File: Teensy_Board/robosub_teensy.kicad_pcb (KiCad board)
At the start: 2 copper layers, 51 parts, among them IC1 TEENSY_4.1, J1 Conn_01x03_Pin, J10 Conn_01x02_Pin, J11 Conn_01x02_Pin, J12 Conn_01x04_Pin, J13 Conn_01x04_Pin, J14 Conn_01x04_Pin, J15 Conn_01x04_Pin, J16 Conn_01x04_Pin, J17 Conn_01x04_Pin, J18 Conn_01x04_Pin, J19 Conn_01x04_Pin, J2 Conn_01x03_Pin, J20 Conn_01x04_Pin, J21 Conn_01x04_Pin, J22 Conn_01x06_Pin, J23 Conn_01x06_Pin, J24 Conn_01x06_Pin, J25 Conn_01x01_Pin, J26 Conn_01x01_Pin, J27 Conn_01x01_Pin, J28 Conn_01x01_Pin, J29 Conn_01x01_Pin, J3 Conn_01x03_Pin, J30 Conn_01x01_Pin, J31 Conn_01x01_Pin, J32 Conn_01x01_Pin, J33 Conn_01x01_Pin, J34 Conn_01x01_Pin, J35 Conn_01x01_Pin, J36 Conn_01x01_Pin, J37 Conn_01x01_Pin, J38 Conn_01x01_Pin, J39 Conn_01x01_Pin, J4 Conn_01x03_Pin, J40 Conn_01x01_Pin, J41 Conn_01x01_Pin, J42 Conn_01x01_Pin, J43 Conn_01x01_Pin, J44 Conn_01x01_Pin, J45 Conn_01x01_Pin, J46 Conn_01x01_Pin, J47 Conn_01x01_Pin, J48 Conn_01x10_Pin, J49 Conn_01x10_Pin, J5 Conn_01x03_Pin, J50 Conn_01x10_Pin, J6 Conn_01x03_Pin, J7 Conn_01x03_Pin, J8 Conn_01x03_Pin, J9 Conn_01x02_Pin

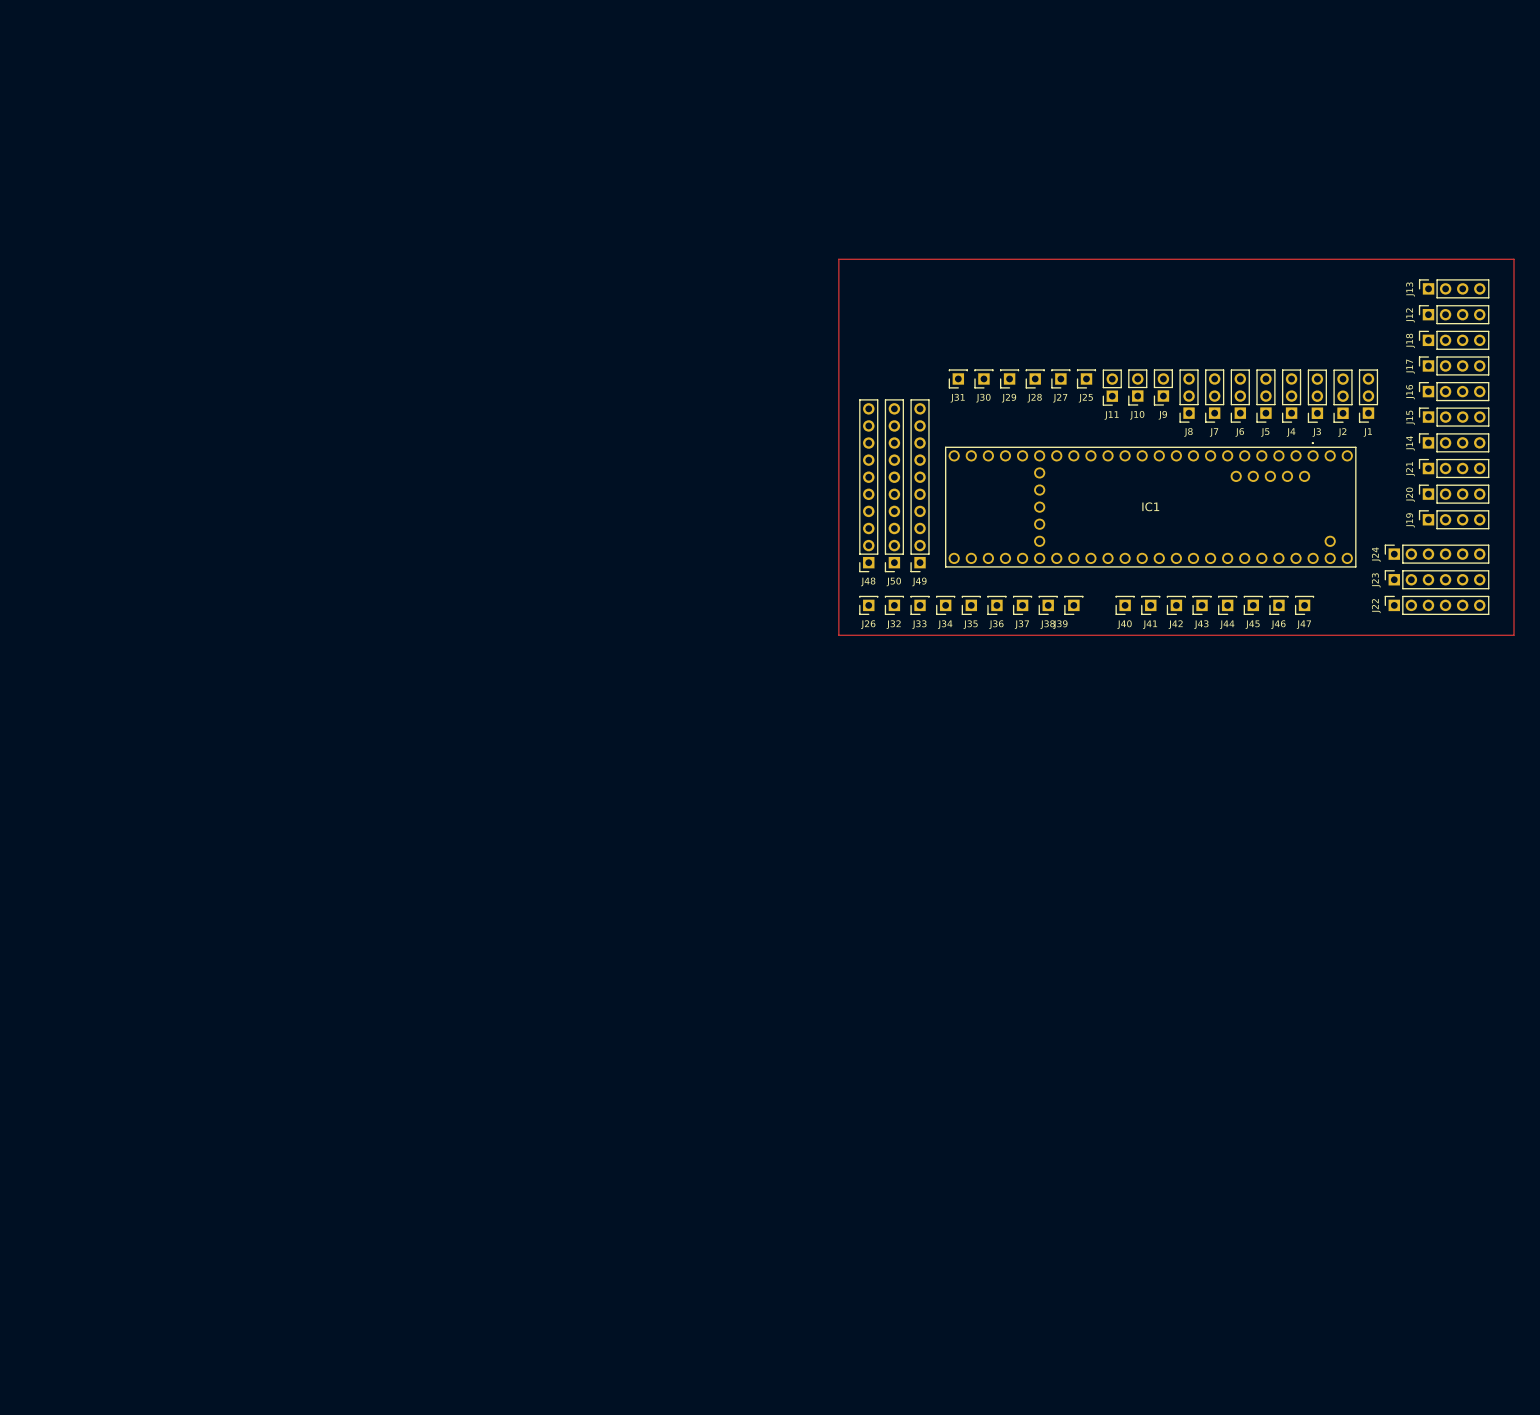
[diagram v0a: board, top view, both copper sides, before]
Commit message: teensy board schematic
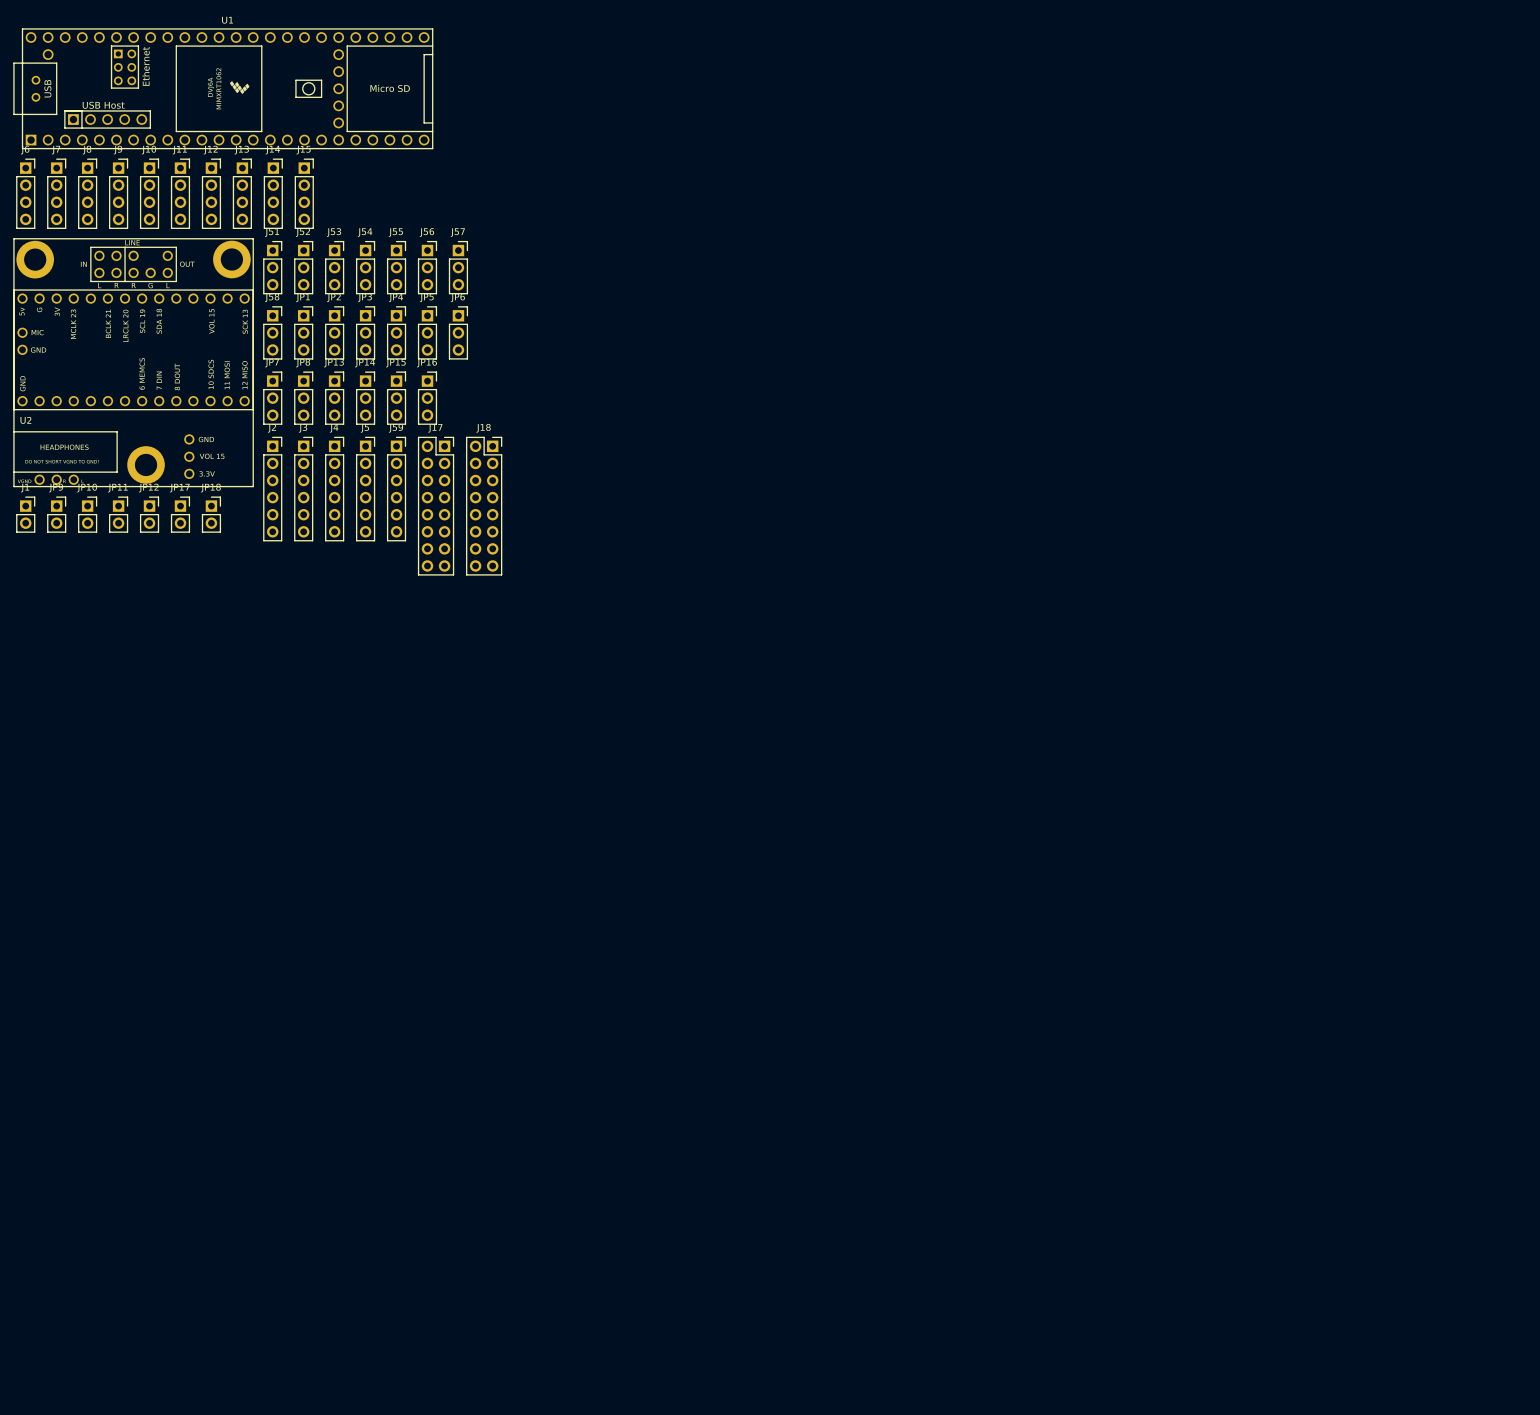
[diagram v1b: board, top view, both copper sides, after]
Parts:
- removed IC1: TEENSY_4.1, KiCad:TEENSY41
- removed J16, J19, J20, J21: Conn_01x04_Pin, Connector_PinSocket_2.54mm:PinSocket_1x04_P2.54mm_Vertical
- removed J22, J23, J24: Conn_01x06_Pin, Connector_PinSocket_2.54mm:PinSocket_1x06_P2.54mm_Vertical
- removed J25, J26, J27, J28, J29, J30, J31, J32, J33, J34, J35, J36, J37, J38, J39, J40, J41, J42, J43, J44, J45, J46, J47: Conn_01x01_Pin, Connector_PinSocket_2.54mm:PinSocket_1x01_P2.54mm_Vertical
- removed J48, J49, J50: Conn_01x10_Pin, Connector_PinSocket_2.54mm:PinSocket_1x10_P2.54mm_Vertical
- added J51: Thruster_1, Connector_PinSocket_2.54mm:PinSocket_1x03_P2.54mm_Vertical, F.Cu at (66.4, 52.7)
- added J52: Thruster_2, Connector_PinSocket_2.54mm:PinSocket_1x03_P2.54mm_Vertical, F.Cu at (71.0, 52.7)
- added J53: Thruster_3, Connector_PinSocket_2.54mm:PinSocket_1x03_P2.54mm_Vertical, F.Cu at (75.6, 52.7)
- added J54: Thruster_6, Connector_PinSocket_2.54mm:PinSocket_1x03_P2.54mm_Vertical, F.Cu at (80.2, 52.7)
- added J55: Thruster_5, Connector_PinSocket_2.54mm:PinSocket_1x03_P2.54mm_Vertical, F.Cu at (84.8, 52.7)
- added J56: Thruster_4, Connector_PinSocket_2.54mm:PinSocket_1x03_P2.54mm_Vertical, F.Cu at (89.4, 52.7)
- added J57: Thruster_8, Connector_PinSocket_2.54mm:PinSocket_1x03_P2.54mm_Vertical, F.Cu at (94.0, 52.7)
- added J58: Thruster_7, Connector_PinSocket_2.54mm:PinSocket_1x03_P2.54mm_Vertical, F.Cu at (66.4, 62.4)
- added J59: PixHawk PM02, Connector_PinSocket_2.54mm:PinSocket_1x06_P2.54mm_Vertical, F.Cu at (84.8, 81.8)
- added JP1: Jumper_3_Bridged12, Connector_PinSocket_2.54mm:PinSocket_1x03_P2.54mm_Vertical, F.Cu at (71.0, 62.4)
- added JP10: Jumper_2_Open, Connector_PinSocket_2.54mm:PinSocket_1x02_P2.54mm_Vertical, F.Cu at (38.9, 90.7)
- added JP11: Jumper_2_Open, Connector_PinSocket_2.54mm:PinSocket_1x02_P2.54mm_Vertical, F.Cu at (43.5, 90.7)
- added JP12: Jumper_2_Open, Connector_PinSocket_2.54mm:PinSocket_1x02_P2.54mm_Vertical, F.Cu at (48.0, 90.7)
- added JP13: Jumper_3_Bridged12, Connector_PinSocket_2.54mm:PinSocket_1x03_P2.54mm_Vertical, F.Cu at (75.6, 72.1)
- added JP14: Jumper_3_Bridged12, Connector_PinSocket_2.54mm:PinSocket_1x03_P2.54mm_Vertical, F.Cu at (80.2, 72.1)
- added JP15: Jumper_3_Bridged12, Connector_PinSocket_2.54mm:PinSocket_1x03_P2.54mm_Vertical, F.Cu at (84.8, 72.1)
- added JP16: Jumper_3_Bridged12, Connector_PinSocket_2.54mm:PinSocket_1x03_P2.54mm_Vertical, F.Cu at (89.4, 72.1)
- added JP17: Jumper_2_Open, Connector_PinSocket_2.54mm:PinSocket_1x02_P2.54mm_Vertical, F.Cu at (52.6, 90.7)
- added JP18: Jumper_2_Open, Connector_PinSocket_2.54mm:PinSocket_1x02_P2.54mm_Vertical, F.Cu at (57.2, 90.7)
- added JP2: Jumper_3_Bridged12, Connector_PinSocket_2.54mm:PinSocket_1x03_P2.54mm_Vertical, F.Cu at (75.6, 62.4)
- added JP3: Jumper_3_Bridged12, Connector_PinSocket_2.54mm:PinSocket_1x03_P2.54mm_Vertical, F.Cu at (80.2, 62.4)
- added JP4: Jumper_3_Bridged12, Connector_PinSocket_2.54mm:PinSocket_1x03_P2.54mm_Vertical, F.Cu at (84.8, 62.4)
- added JP5: Jumper_3_Bridged12, Connector_PinSocket_2.54mm:PinSocket_1x03_P2.54mm_Vertical, F.Cu at (89.4, 62.4)
- added JP6: Jumper_3_Bridged12, Connector_PinSocket_2.54mm:PinSocket_1x03_P2.54mm_Vertical, F.Cu at (94.0, 62.4)
- added JP7: Jumper_3_Bridged12, Connector_PinSocket_2.54mm:PinSocket_1x03_P2.54mm_Vertical, F.Cu at (66.4, 72.1)
- added JP8: Jumper_3_Bridged12, Connector_PinSocket_2.54mm:PinSocket_1x03_P2.54mm_Vertical, F.Cu at (71.0, 72.1)
- added JP9: Jumper_2_Open, Connector_PinSocket_2.54mm:PinSocket_1x02_P2.54mm_Vertical, F.Cu at (34.2, 90.7)
- added U1: Teensy4.1, teensy:Teensy41, F.Cu at (59.6, 28.6)
- added U2: Teensy4.0_AudioShield_REVD, teensy_audio_shield:4.0audioshield, F.Cu at (29.2, 75.0)
- J1: value Conn_01x03_Pin -> UART; footprint Connector_PinSocket_2.54mm:PinSocket_1x03_P2.54mm_Vertical -> Connector_PinSocket_2.54mm:PinSocket_1x02_P2.54mm_Vertical
- J10: value Conn_01x02_Pin -> I2C1_BUS5; footprint Connector_PinSocket_2.54mm:PinSocket_1x02_P2.54mm_Vertical -> Connector_PinSocket_2.54mm:PinSocket_1x04_P2.54mm_Vertical
- J11: value Conn_01x02_Pin -> I2C1_BUS7; footprint Connector_PinSocket_2.54mm:PinSocket_1x02_P2.54mm_Vertical -> Connector_PinSocket_2.54mm:PinSocket_1x04_P2.54mm_Vertical
- J12: value Conn_01x04_Pin -> I2C1_BUS6
- J13: value Conn_01x04_Pin -> I2C1_BUS8
- J14: value Conn_01x04_Pin -> I2C2_BUS1
- J15: value Conn_01x04_Pin -> I2C3_BUS1
- J17: value Conn_01x04_Pin -> 3.3V Power; footprint Connector_PinSocket_2.54mm:PinSocket_1x04_P2.54mm_Vertical -> Connector_PinSocket_2.54mm:PinSocket_2x08_P2.54mm_Vertical
- J18: value Conn_01x04_Pin -> 5V Power; footprint Connector_PinSocket_2.54mm:PinSocket_1x04_P2.54mm_Vertical -> Connector_PinSocket_2.54mm:PinSocket_2x08_P2.54mm_Vertical
- J2: value Conn_01x03_Pin -> SPI_BUS1; footprint Connector_PinSocket_2.54mm:PinSocket_1x03_P2.54mm_Vertical -> Connector_PinSocket_2.54mm:PinSocket_1x06_P2.54mm_Vertical
- J3: value Conn_01x03_Pin -> SPI_BUS2; footprint Connector_PinSocket_2.54mm:PinSocket_1x03_P2.54mm_Vertical -> Connector_PinSocket_2.54mm:PinSocket_1x06_P2.54mm_Vertical
- J4: value Conn_01x03_Pin -> SPI_BUS3; footprint Connector_PinSocket_2.54mm:PinSocket_1x03_P2.54mm_Vertical -> Connector_PinSocket_2.54mm:PinSocket_1x06_P2.54mm_Vertical
- J5: value Conn_01x03_Pin -> SPI_BUS4; footprint Connector_PinSocket_2.54mm:PinSocket_1x03_P2.54mm_Vertical -> Connector_PinSocket_2.54mm:PinSocket_1x06_P2.54mm_Vertical
- J6: value Conn_01x03_Pin -> I2C1_BUS1; footprint Connector_PinSocket_2.54mm:PinSocket_1x03_P2.54mm_Vertical -> Connector_PinSocket_2.54mm:PinSocket_1x04_P2.54mm_Vertical
- J7: value Conn_01x03_Pin -> I2C1_BUS2; footprint Connector_PinSocket_2.54mm:PinSocket_1x03_P2.54mm_Vertical -> Connector_PinSocket_2.54mm:PinSocket_1x04_P2.54mm_Vertical
- J8: value Conn_01x03_Pin -> I2C1_BUS3; footprint Connector_PinSocket_2.54mm:PinSocket_1x03_P2.54mm_Vertical -> Connector_PinSocket_2.54mm:PinSocket_1x04_P2.54mm_Vertical
- J9: value Conn_01x02_Pin -> I2C1_BUS4; footprint Connector_PinSocket_2.54mm:PinSocket_1x02_P2.54mm_Vertical -> Connector_PinSocket_2.54mm:PinSocket_1x04_P2.54mm_Vertical
- moved J1 200.0 mm to (29.6, 90.7), turned to 0 degrees
- moved J6 184.1 mm to (29.6, 40.4), turned to 0 degrees
- moved J12 182.2 mm to (57.2, 40.4), turned to 0 degrees
- moved J13 177.2 mm to (61.9, 40.4), turned to 0 degrees
- moved J14 176.5 mm to (66.5, 40.4), turned to 0 degrees
- moved J7 175.9 mm to (34.2, 40.4), turned to 0 degrees
- moved J15 171.1 mm to (71.0, 40.4), turned to 0 degrees
- moved J8 167.7 mm to (38.9, 40.4), turned to 0 degrees
- moved J2 159.1 mm to (66.4, 81.8), turned to 0 degrees
- moved J9 158.9 mm to (43.5, 40.4), turned to 0 degrees
- moved J3 150.7 mm to (71.0, 81.8), turned to 0 degrees
- moved J10 150.7 mm to (48.0, 40.4), turned to 0 degrees
- moved J17 146.7 mm to (91.9, 81.8), turned to 0 degrees
- moved J11 142.6 mm to (52.6, 40.4), turned to 0 degrees
- moved J4 142.3 mm to (75.6, 81.8), turned to 0 degrees
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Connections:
- J1 pad 1: Net-(IC1-OUT2) -> UART_RX
- J1 pad 2: unconnected-(J1-Pin_2-Pad2) -> UART_TX
- J10 pad 1: Net-(IC1-A11) -> +3.3V
- J10 pad 2: Net-(IC1-GND_6) -> I2C1_SCL
- J11 pad 1: Net-(IC1-A12) -> +3.3V
- J11 pad 2: Net-(IC1-GND_6) -> I2C1_SCL
- J12 pad 1: Net-(IC1-A4) -> +3.3V
- J12 pad 2: Net-(IC1-A5) -> I2C1_SCL
- J12 pad 3: Net-(IC1-3.3V_1) -> I2C1_SDA
- J12 pad 4: Net-(IC1-GND_6) -> GND
- J13 pad 1: Net-(IC1-A4) -> +3.3V
- J13 pad 2: Net-(IC1-A5) -> I2C1_SCL
- J13 pad 3: Net-(IC1-3.3V_1) -> I2C1_SDA
- J13 pad 4: Net-(IC1-GND_6) -> GND
- J14 pad 1: Net-(IC1-A4) -> Net-(J14-Pin_1)
- J14 pad 2: Net-(IC1-A5) -> I2C2_SCL
- J14 pad 3: Net-(IC1-3.3V_1) -> I2C2_SDA
- J14 pad 4: Net-(IC1-GND_6) -> GND
- J15 pad 1: Net-(IC1-A4) -> Net-(J15-Pin_1)
- J15 pad 2: Net-(IC1-A5) -> I2C3_SCL
- J15 pad 3: Net-(IC1-3.3V_1) -> I2C3_SDA
- J15 pad 4: Net-(IC1-GND_6) -> GND
- J17 pad 1: Net-(IC1-A4) -> +3.3V
- J17 pad 2: Net-(IC1-A5) -> +3.3V
- J17 pad 3: Net-(IC1-3.3V_1) -> +3.3V
- J17 pad 4: Net-(IC1-GND_6) -> +3.3V
- J18 pad 1: Net-(IC1-A4) -> +5V
- J18 pad 2: Net-(IC1-A5) -> +5V
- J18 pad 3: Net-(IC1-3.3V_1) -> +5V
- J18 pad 4: Net-(IC1-GND_6) -> +5V
- J2 pad 2: unconnected-(J2-Pin_2-Pad2) -> SPI_MOSI
- J2 pad 3: Net-(IC1-GND_6) -> SPI_MISO
- J3 pad 2: unconnected-(J3-Pin_2-Pad2) -> SPI_MOSI
- J3 pad 3: Net-(IC1-GND_6) -> SPI_MISO
- J4 pad 1: Net-(IC1-IN2) -> +3.3V
- J4 pad 2: unconnected-(J4-Pin_2-Pad2) -> SPI_MOSI
- J4 pad 3: Net-(IC1-GND_6) -> SPI_MISO
- J5 pad 1: Net-(IC1-OUT1D) -> +3.3V
- J5 pad 2: unconnected-(J5-Pin_2-Pad2) -> SPI_MOSI
- J5 pad 3: Net-(IC1-GND_6) -> SPI_MISO
- J6 pad 2: unconnected-(J6-Pin_2-Pad2) -> I2C1_SCL
- J6 pad 3: Net-(IC1-GND_6) -> I2C1_SDA
- J7 pad 2: unconnected-(J7-Pin_2-Pad2) -> I2C1_SCL
- J7 pad 3: Net-(IC1-GND_6) -> I2C1_SDA
- J8 pad 2: unconnected-(J8-Pin_2-Pad2) -> I2C1_SCL
- J8 pad 3: Net-(IC1-GND_6) -> I2C1_SDA
- J9 pad 2: Net-(IC1-GND_6) -> I2C1_SCL

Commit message: v1 ok2fab
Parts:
- removed J15: I2C3_BUS1, Connector_PinSocket_2.54mm:PinSocket_1x04_P2.54mm_Vertical
- removed J51: Thruster_1, Connector_PinSocket_2.54mm:PinSocket_1x03_P2.54mm_Vertical
- removed J52: Thruster_2, Connector_PinSocket_2.54mm:PinSocket_1x03_P2.54mm_Vertical
- removed J53: Thruster_3, Connector_PinSocket_2.54mm:PinSocket_1x03_P2.54mm_Vertical
- removed J54: Thruster_6, Connector_PinSocket_2.54mm:PinSocket_1x03_P2.54mm_Vertical
- removed J55: Thruster_5, Connector_PinSocket_2.54mm:PinSocket_1x03_P2.54mm_Vertical
- removed J56: Thruster_4, Connector_PinSocket_2.54mm:PinSocket_1x03_P2.54mm_Vertical
- removed J57: Thruster_8, Connector_PinSocket_2.54mm:PinSocket_1x03_P2.54mm_Vertical
- removed J58: Thruster_7, Connector_PinSocket_2.54mm:PinSocket_1x03_P2.54mm_Vertical
- removed J59: PixHawk PM02, Connector_PinSocket_2.54mm:PinSocket_1x06_P2.54mm_Vertical
- removed JP5, JP6: Jumper_3_Bridged12, Connector_PinSocket_2.54mm:PinSocket_1x03_P2.54mm_Vertical
- added H1: MountingHole, MountingHole:MountingHole_3.2mm_M3, F.Cu at (135.8, 167.2)
- added H2: MountingHole, MountingHole:MountingHole_3.2mm_M3, F.Cu at (195.8, 212.2)
- added H3: MountingHole, MountingHole:MountingHole_3.2mm_M3, F.Cu at (240.8, 212.2)
- added J19: BUS4, Connector_PinSocket_2.54mm:PinSocket_1x04_P2.54mm_Vertical, F.Cu at (245.8, 162.1)
- added J20: BUS5, Connector_PinSocket_2.54mm:PinSocket_1x04_P2.54mm_Vertical, F.Cu at (153.3, 161.4)
- added J21: BUS6, Connector_PinSocket_2.54mm:PinSocket_1x04_P2.54mm_Vertical, F.Cu at (157.3, 161.4)
- added J22: SPI1, Connector_PinSocket_2.54mm:PinSocket_1x06_P2.54mm_Vertical, F.Cu at (181.2, 161.5)
- added J23: SPI2, Connector_PinSocket_2.54mm:PinSocket_1x06_P2.54mm_Vertical, F.Cu at (185.8, 161.5)
- added J24: I2C_2, Connector_PinSocket_2.54mm:PinSocket_1x04_P2.54mm_Vertical, F.Cu at (165.1, 161.3)
- added J25: I2C_3, Connector_PinSocket_2.54mm:PinSocket_1x04_P2.54mm_Vertical, F.Cu at (169.1, 161.3)
- added J26: SPI3, Connector_PinSocket_2.54mm:PinSocket_1x06_P2.54mm_Vertical, F.Cu at (190.5, 161.5)
- added J27: SPI4, Connector_PinSocket_2.54mm:PinSocket_1x06_P2.54mm_Vertical, F.Cu at (195.1, 161.5)
- J1: value UART -> T1; footprint Connector_PinSocket_2.54mm:PinSocket_1x02_P2.54mm_Vertical -> Connector_PinSocket_2.54mm:PinSocket_1x03_P2.54mm_Vertical
- J10: value I2C1_BUS5 -> PixHawk PM02; footprint Connector_PinSocket_2.54mm:PinSocket_1x04_P2.54mm_Vertical -> Connector_PinSocket_2.54mm:PinSocket_1x06_P2.54mm_Vertical
- J11: value I2C1_BUS7 -> 3.3V Power; footprint Connector_PinSocket_2.54mm:PinSocket_1x04_P2.54mm_Vertical -> Connector_PinSocket_2.54mm:PinSocket_2x08_P2.54mm_Vertical
- J12: value I2C1_BUS6 -> 5V Power; footprint Connector_PinSocket_2.54mm:PinSocket_1x04_P2.54mm_Vertical -> Connector_PinSocket_2.54mm:PinSocket_2x08_P2.54mm_Vertical
- J13: value I2C1_BUS8 -> BUS1
- J14: value I2C2_BUS1 -> BUS2
- J17: value 3.3V Power -> Digital Pins; footprint Connector_PinSocket_2.54mm:PinSocket_2x08_P2.54mm_Vertical -> Connector_PinSocket_2.54mm:PinSocket_2x11_P2.54mm_Vertical
- J18: value 5V Power -> BUS3; footprint Connector_PinSocket_2.54mm:PinSocket_2x08_P2.54mm_Vertical -> Connector_PinSocket_2.54mm:PinSocket_1x04_P2.54mm_Vertical
- J2: value SPI_BUS1 -> UART; footprint Connector_PinSocket_2.54mm:PinSocket_1x06_P2.54mm_Vertical -> Connector_PinSocket_2.54mm:PinSocket_1x02_P2.54mm_Vertical
- J3: value SPI_BUS2 -> T2; footprint Connector_PinSocket_2.54mm:PinSocket_1x06_P2.54mm_Vertical -> Connector_PinSocket_2.54mm:PinSocket_1x03_P2.54mm_Vertical
- J4: value SPI_BUS3 -> T6; footprint Connector_PinSocket_2.54mm:PinSocket_1x06_P2.54mm_Vertical -> Connector_PinSocket_2.54mm:PinSocket_1x03_P2.54mm_Vertical
- J5: value SPI_BUS4 -> T3; footprint Connector_PinSocket_2.54mm:PinSocket_1x06_P2.54mm_Vertical -> Connector_PinSocket_2.54mm:PinSocket_1x03_P2.54mm_Vertical
- J6: value I2C1_BUS1 -> T7; footprint Connector_PinSocket_2.54mm:PinSocket_1x04_P2.54mm_Vertical -> Connector_PinSocket_2.54mm:PinSocket_1x03_P2.54mm_Vertical
- J7: value I2C1_BUS2 -> T4; footprint Connector_PinSocket_2.54mm:PinSocket_1x04_P2.54mm_Vertical -> Connector_PinSocket_2.54mm:PinSocket_1x03_P2.54mm_Vertical
- J8: value I2C1_BUS3 -> T8; footprint Connector_PinSocket_2.54mm:PinSocket_1x04_P2.54mm_Vertical -> Connector_PinSocket_2.54mm:PinSocket_1x03_P2.54mm_Vertical
- J9: value I2C1_BUS4 -> T5; footprint Connector_PinSocket_2.54mm:PinSocket_1x04_P2.54mm_Vertical -> Connector_PinSocket_2.54mm:PinSocket_1x03_P2.54mm_Vertical
- JP1: value Jumper_3_Bridged12 -> BUS1_PWR
- JP10: value Jumper_2_Open -> I2C3_PWR; footprint Connector_PinSocket_2.54mm:PinSocket_1x02_P2.54mm_Vertical -> Connector_PinSocket_2.54mm:PinSocket_1x03_P2.54mm_Vertical
- JP11: value Jumper_2_Open -> AUDIO_DIN; footprint Connector_PinSocket_2.54mm:PinSocket_1x02_P2.54mm_Vertical -> Jumper:SolderJumper-2_P1.3mm_Open_Pad1.0x1.5mm; moved to B.Cu
- JP12: value Jumper_2_Open -> AUDIO_DOUT; footprint Connector_PinSocket_2.54mm:PinSocket_1x02_P2.54mm_Vertical -> Jumper:SolderJumper-2_P1.3mm_Open_Pad1.0x1.5mm; moved to B.Cu
- JP13: value Jumper_3_Bridged12 -> AUDIO_CS; footprint Connector_PinSocket_2.54mm:PinSocket_1x03_P2.54mm_Vertical -> Jumper:SolderJumper-2_P1.3mm_Open_Pad1.0x1.5mm; moved to B.Cu
- JP14: value Jumper_3_Bridged12 -> AUDIO_MOSI; footprint Connector_PinSocket_2.54mm:PinSocket_1x03_P2.54mm_Vertical -> Jumper:SolderJumper-2_P1.3mm_Open_Pad1.0x1.5mm; moved to B.Cu
- JP15: value Jumper_3_Bridged12 -> AUDIO_MISO; footprint Connector_PinSocket_2.54mm:PinSocket_1x03_P2.54mm_Vertical -> Jumper:SolderJumper-2_P1.3mm_Open_Pad1.0x1.5mm; moved to B.Cu
- JP16: value Jumper_3_Bridged12 -> AUDIO_SCK; footprint Connector_PinSocket_2.54mm:PinSocket_1x03_P2.54mm_Vertical -> Jumper:SolderJumper-2_P1.3mm_Open_Pad1.0x1.5mm; moved to B.Cu
- JP17: value Jumper_2_Open -> SDA_Sel; footprint Connector_PinSocket_2.54mm:PinSocket_1x02_P2.54mm_Vertical -> Connector_PinSocket_2.54mm:PinSocket_1x03_P2.54mm_Vertical
- JP18: value Jumper_2_Open -> SCL_Sel; footprint Connector_PinSocket_2.54mm:PinSocket_1x02_P2.54mm_Vertical -> Connector_PinSocket_2.54mm:PinSocket_1x03_P2.54mm_Vertical
- JP2: value Jumper_3_Bridged12 -> BUS2_PWR
- JP3: value Jumper_3_Bridged12 -> T6_Sel
- JP4: value Jumper_3_Bridged12 -> T7_Sel
- JP7: value Jumper_3_Bridged12 -> SPI1_PWR
- JP8: value Jumper_3_Bridged12 -> SPI2_PWR
- JP9: value Jumper_2_Open -> I2C2_PWR; footprint Connector_PinSocket_2.54mm:PinSocket_1x02_P2.54mm_Vertical -> Connector_PinSocket_2.54mm:PinSocket_1x03_P2.54mm_Vertical
- moved J7 251.6 mm to (220.4, 209.6)
- moved J11 247.8 mm to (240.6, 202.0), turned to 180 degrees
- moved J6 246.1 mm to (208.3, 209.6)
- moved J9 241.9 mm to (216.4, 209.6)
- moved J8 236.7 mm to (204.3, 209.6)
- moved J1 235.1 mm to (232.4, 209.6)
- moved JP17 205.1 mm to (227.0, 198.7)
- moved JP18 204.9 mm to (231.4, 198.7)
- moved JP11 204.5 mm to (231.9, 170.0), turned to 180 degrees
- moved U2 203.2 mm to (202.2, 181.5)
- moved J3 202.8 mm to (228.4, 209.6)
- moved JP12 202.1 mm to (231.9, 174.4), turned to 180 degrees
- moved U1 198.8 mm to (160.3, 200.1)
- moved JP3 193.4 mm to (212.4, 203.6), turned to 180 degrees
- moved J5 192.8 mm to (224.4, 209.6)
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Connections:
- J1 pad 1: UART_RX -> PWM2
- J1 pad 2: UART_TX -> unconnected-(J1-Pin_2-Pad2)
- J10 pad 1: +3.3V -> +5V
- J10 pad 2: I2C1_SCL -> +5V
- J10 pad 3: I2C1_SDA -> Analog_Current
- J10 pad 4: GND -> Analog_Voltage
- J11 pad 1: +3.3V -> GND
- J11 pad 2: I2C1_SCL -> +3.3V
- J11 pad 3: I2C1_SDA -> GND
- J11 pad 4: GND -> +3.3V
- J12 pad 1: +3.3V -> GND
- J12 pad 2: I2C1_SCL -> +5V
- J12 pad 3: I2C1_SDA -> GND
- J12 pad 4: GND -> +5V
- J13 pad 1: +3.3V -> Net-(J13-Pin_1)
- J14 pad 2: I2C2_SCL -> I2C1_SCL
- J14 pad 3: I2C2_SDA -> I2C1_SDA
- J17 pad 1: +3.3V -> GND
- J17 pad 10: GND -> D5
- J17 pad 12: GND -> D6
- J17 pad 14: GND -> D7
- J17 pad 16: GND -> D8/A3/PWM12
- J17 pad 2: +3.3V -> D1/A1
- J17 pad 3: +3.3V -> GND
- J17 pad 4: +3.3V -> D2/A2
- J17 pad 5: +3.3V -> GND
- J17 pad 6: +3.3V -> D3/PWM10
- J17 pad 7: +3.3V -> GND
- J17 pad 8: +3.3V -> D4/PWM11
- J18 pad 1: +5V -> +3.3V
- J18 pad 2: +5V -> I2C1_SCL
- J18 pad 3: +5V -> I2C1_SDA
- J18 pad 4: +5V -> GND
- J2 pad 1: Net-(J2-Pin_1) -> UART_RX
- J2 pad 2: SPI_MOSI -> UART_TX
- J3 pad 1: Net-(J3-Pin_1) -> PWM3
- J3 pad 2: SPI_MOSI -> unconnected-(J3-Pin_2-Pad2)
- J3 pad 3: SPI_MISO -> GND
- J4 pad 1: +3.3V -> Net-(J4-Pin_1)
- J4 pad 2: SPI_MOSI -> unconnected-(J4-Pin_2-Pad2)
- J4 pad 3: SPI_MISO -> GND
- J5 pad 1: +3.3V -> PWM4
- J5 pad 2: SPI_MOSI -> unconnected-(J5-Pin_2-Pad2)
- J5 pad 3: SPI_MISO -> GND
- J6 pad 2: I2C1_SCL -> unconnected-(J6-Pin_2-Pad2)
- J6 pad 3: I2C1_SDA -> GND
- J7 pad 1: Net-(J7-Pin_1) -> PWM5
- J7 pad 2: I2C1_SCL -> unconnected-(J7-Pin_2-Pad2)
- J7 pad 3: I2C1_SDA -> GND
- J8 pad 1: Net-(J8-Pin_1) -> PWM9
- J8 pad 2: I2C1_SCL -> unconnected-(J8-Pin_2-Pad2)
- J8 pad 3: I2C1_SDA -> GND
- J9 pad 1: Net-(J9-Pin_1) -> PWM6
- J9 pad 2: I2C1_SCL -> unconnected-(J9-Pin_2-Pad2)
- J9 pad 3: I2C1_SDA -> GND
- JP1 pad 2: Net-(J2-Pin_1) -> Net-(J13-Pin_1)
- JP10 pad 1: SPI_MOSI -> +3.3V
- JP10 pad 2: Net-(JP10-B) -> Net-(J25-Pin_1)
- JP11 pad 1: SPI_MISO -> PWM7/AUDIO_DIN
- JP12 pad 1: SPI_SCK -> PWM8/AUDIO_DOUT
- JP13 pad 1: I2C2_SDA -> SPI_CS4
- JP13 pad 2: Net-(JP13-C) -> Net-(JP13-B)
- JP14 pad 1: I2C2_SCL -> SPI_MOSI
- JP14 pad 2: Net-(JP14-C) -> Net-(JP14-B)
- JP15 pad 1: PWM0 -> SPI_MISO
- JP15 pad 2: Net-(J54-Pin_1) -> Net-(JP15-B)
- JP16 pad 1: PWM1 -> SPI_SCK
- JP16 pad 2: Net-(J58-Pin_1) -> Net-(JP16-B)
- JP17 pad 1: PWM7/AUDIO_DIN -> I2C2_SDA
- JP17 pad 2: Net-(JP17-B) -> Net-(JP17-C)
- JP18 pad 1: PWM8/AUDIO_DOUT -> I2C2_SCL
- JP18 pad 2: Net-(JP18-B) -> Net-(JP18-C)
- JP2 pad 2: Net-(J3-Pin_1) -> Net-(J14-Pin_1)
- JP3 pad 1: +3.3V -> PWM0
- JP3 pad 2: Net-(J14-Pin_1) -> Net-(J4-Pin_1)
- JP3 pad 3: +5V -> PWM7/AUDIO_DIN
- JP4 pad 1: +3.3V -> PWM1
- JP4 pad 2: Net-(J15-Pin_1) -> Net-(J6-Pin_1)
- JP4 pad 3: +5V -> PWM8/AUDIO_DOUT
- JP7 pad 2: Net-(J8-Pin_1) -> Net-(J22-Pin_1)
- JP8 pad 2: Net-(J9-Pin_1) -> Net-(J23-Pin_1)
- JP9 pad 1: SPI_CS4 -> +3.3V
- JP9 pad 2: Net-(JP9-B) -> Net-(J24-Pin_1)
- U2 pad 10: Net-(JP18-B) -> Net-(JP12-B)
- U2 pad 12: Net-(JP9-B) -> Net-(JP13-B)
- U2 pad 13: Net-(JP10-B) -> Net-(JP14-B)
- U2 pad 14: Net-(JP11-B) -> Net-(JP15-B)
- U2 pad 17: Net-(JP12-B) -> Net-(JP16-B)
- U2 pad 22: Net-(JP13-C) -> Net-(JP17-C)
- U2 pad 23: Net-(JP14-C) -> Net-(JP18-C)
- U2 pad 9: Net-(JP17-B) -> Net-(JP11-B)
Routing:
- net I2C1_SCL: track 0.00 -> 195.9 mm, vias 0 -> 6
- net I2C1_SDA: track 0.00 -> 182.8 mm, vias 0 -> 4
- net PWM7/AUDIO_DIN: track 0.00 -> 127.2 mm, vias 0 -> 3
- net I2C2_SCL: track 0.00 -> 122.0 mm, vias 0 -> 4
- net I2C2_SDA: track 0.00 -> 118.6 mm, vias 0 -> 6
- net Vol_Knob: track 0.00 -> 108.9 mm, vias 0 -> 4
- net MCLK: track 0.00 -> 107.8 mm, vias 0 -> 1
- net PWM2: track 0.00 -> 107.3 mm, vias 0 -> 2
- net PWM8/AUDIO_DOUT: track 0.00 -> 107.1 mm, vias 0 -> 5
- net SPI_MOSI: track 0.00 -> 107.1 mm, vias 0 -> 4
- net LRCLK: track 0.00 -> 106.9 mm, vias 0 -> 3
- net BCLK: track 0.00 -> 106.5 mm, vias 0 -> 2
- net PWM0: track 0.00 -> 100.4 mm, vias 0 -> 1
- net PWM3: track 0.00 -> 99.0 mm, vias 0 -> 2
- net SPI_MISO: track 0.00 -> 95.9 mm, vias 0 -> 1
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- added copper zone on B.Cu, net (none)
- added copper zone on In1.Cu, net +3.3V
- added copper zone on F.Cu, net +5V
- added copper zone on In2.Cu, net GND
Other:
- board outline added: 120 x 64 mm
- copper layers 2 -> 4
- board text added: "3.3V"
- board text added: "5/3"
- board text added: "5V"
- board text added: "AI"
- board text added: "AV"
- board text added: "CS"
- board text added: "D1"
- board text added: "D11"
- board text added: "GND"
- board text added: "I2C1"
- board text added: "I2C2"
- board text added: "MISO"
- board text added: "MOSI"
- board text added: "PWM0"
- board text added: "PWM1"
- board text added: "PWM7"
- board text added: "PWM8"
- board text added: "RX"
- board text added: "SCK"
- board text added: "SCL"
- board text added: "SDA"
- board text added: "Stanford Robosub Microcontroller Breakout Board {dblquote}The tides are in our veins{dblquote} -- Robinson Jeffries"
- board text added: "TX"
